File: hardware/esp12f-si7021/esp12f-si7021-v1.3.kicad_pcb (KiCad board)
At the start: 2 copper layers, 49.9 x 34 mm, 25 parts, among them J1 JST PH3, J2 ESP_01x06_Female, J3 JST PH2, J4 JST GH2, Q1 BSS84, U1 MCP1700-3302E_SOT23, U2 ESP-12F, U3 Si7021-A20

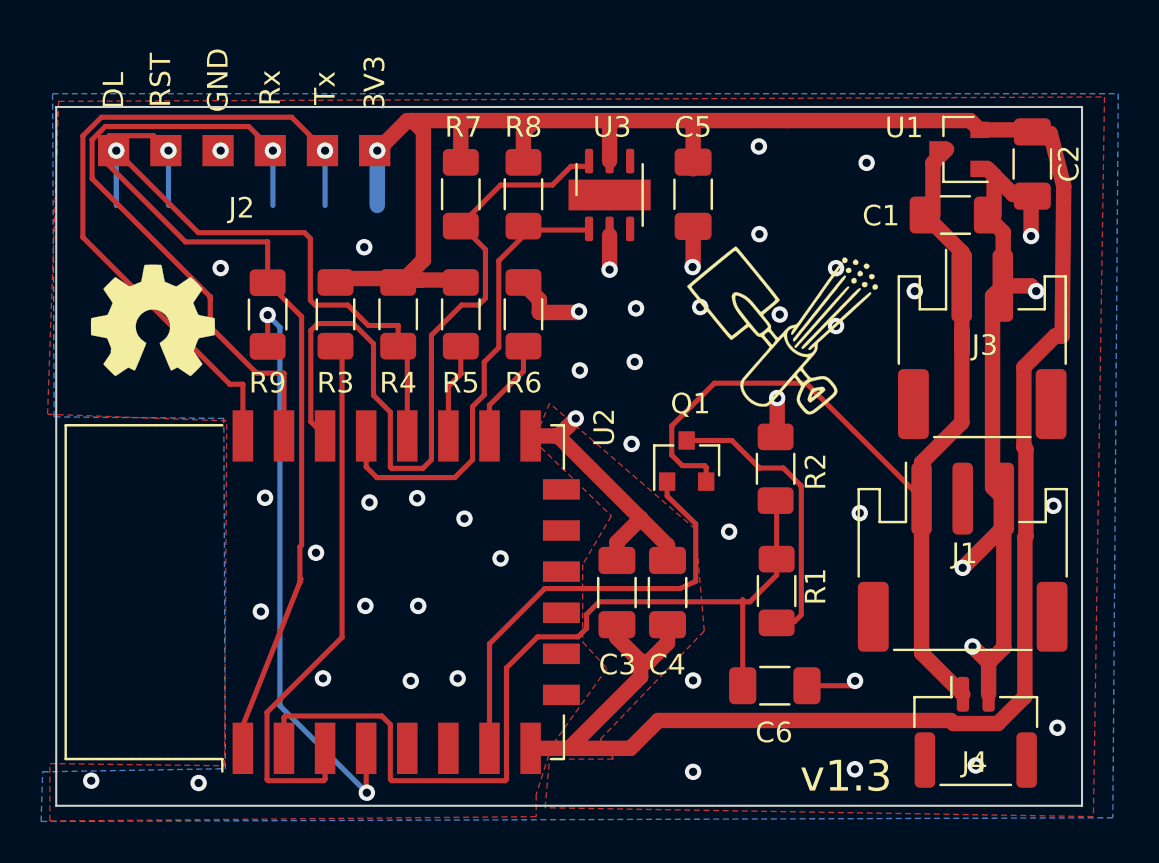
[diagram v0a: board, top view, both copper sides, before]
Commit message: Tweak positioning of programming header
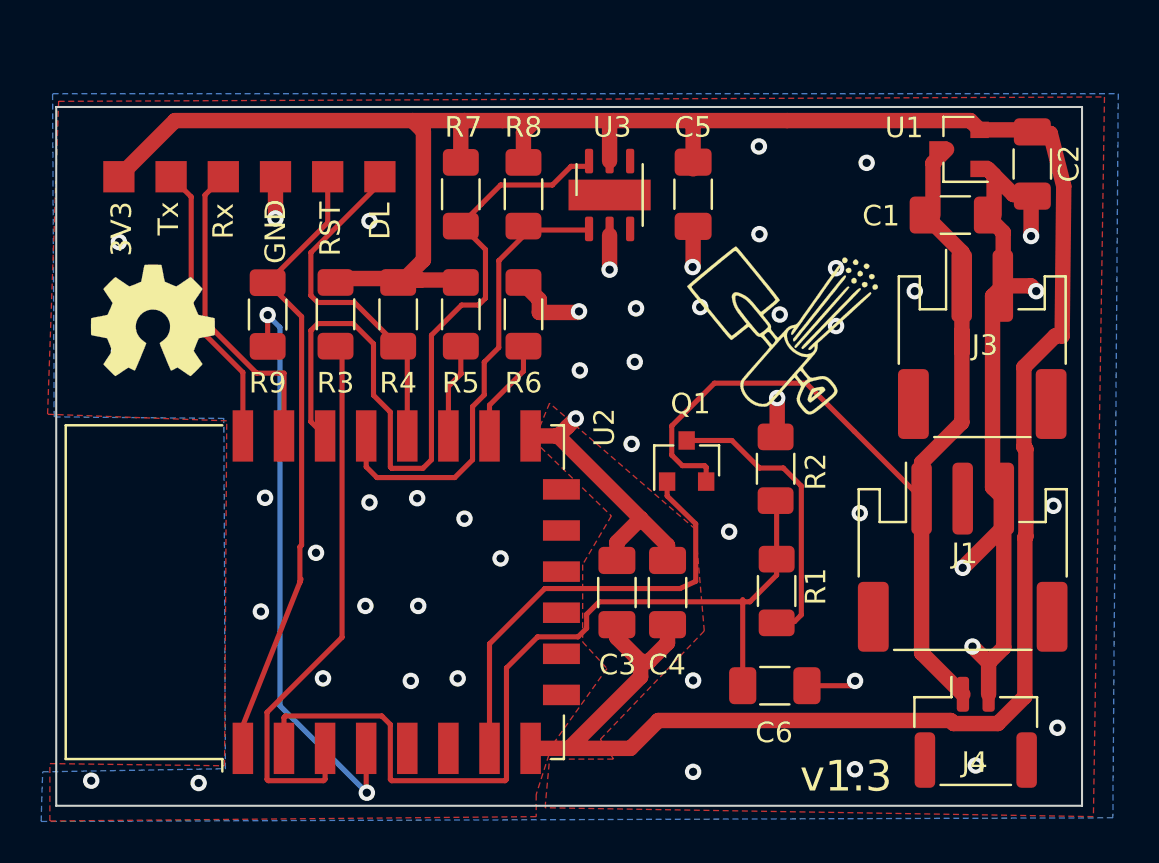
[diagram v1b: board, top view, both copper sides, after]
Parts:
- moved J2 3.82 mm to (23.0, 14.6), turned to 0 degrees
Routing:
- net Net-(J2-Pad2): track 33.7 -> 14.1 mm, vias 1 -> 0
- net Net-(J2-Pad3): track 32.2 -> 16.1 mm, vias 1 -> 0
- net Net-(J2-Pad5): track 42.7 -> 30.2 mm, vias 1 -> 0
- net +3V3: track 124.9 -> 135.3 mm, vias 1 -> 0
- net Net-(J2-Pad6): track 27.7 -> 17.5 mm, vias 1 -> 0
- net GND: track 64.6 -> 66.6 mm
